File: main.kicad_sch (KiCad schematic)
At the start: 0 parts

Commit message: added motor IC
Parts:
- added U1: DRV8833PWPR, DRV8833PWPR:IC_DRV8833PWPR, symbol DRV8833PWPR[1]:DRV8833PWPR

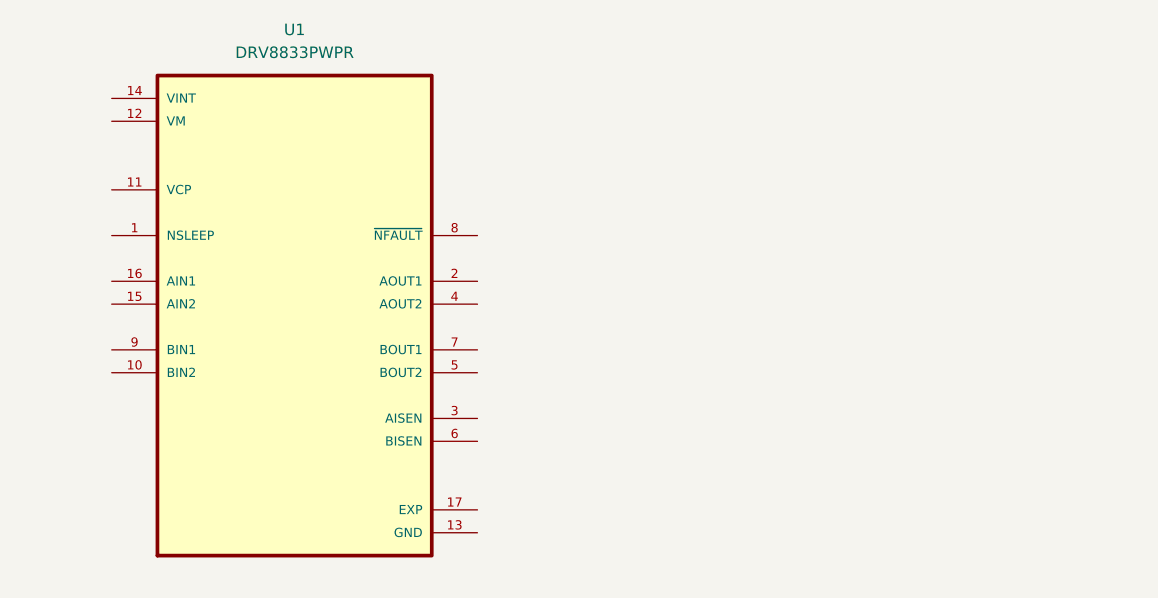
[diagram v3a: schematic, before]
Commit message: DNP for 2x16 and global labels
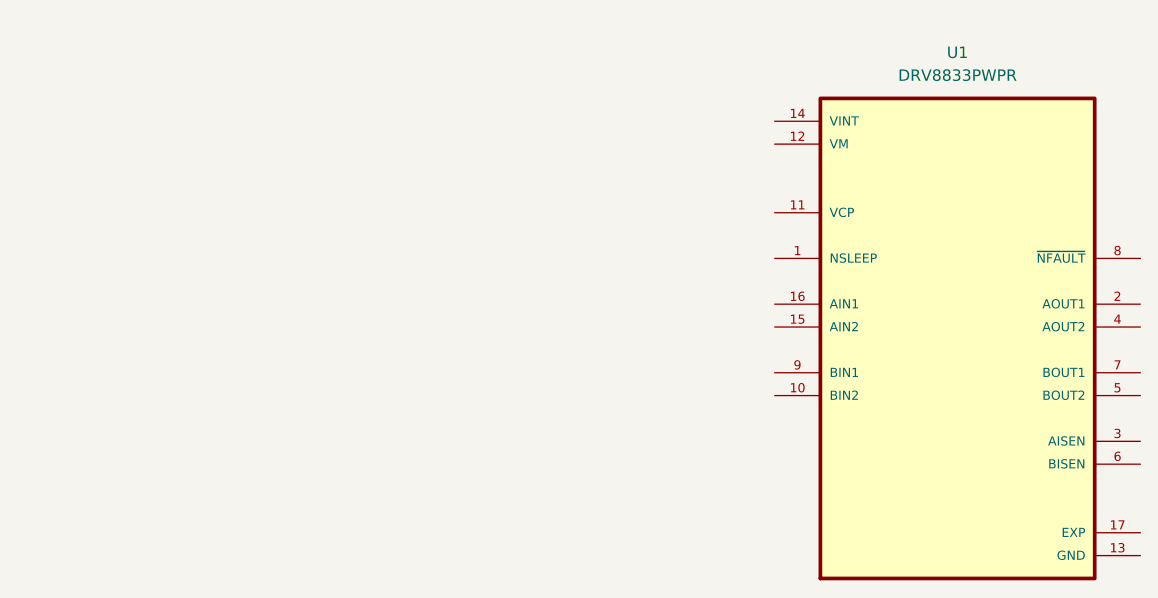
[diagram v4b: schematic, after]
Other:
- moved on the sheet: U1
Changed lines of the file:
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@@
 	(symbol
 		(lib_id "DRV8833PWPR[1]:DRV8833PWPR")
-		(at 87.63 97.79 0)
+		(at 161.29 100.33 0)
 		(unit 1)
 		(exclude_from_sim no)
@@
 		(fields_autoplaced yes)
 		(property "Reference" "U1"
-			(at 87.63 64.77 0)
+			(at 161.29 67.31 0)
 			(effects
 				(font
@@
 		)
 		(property "Value" "DRV8833PWPR"
-			(at 87.63 67.31 0)
+			(at 161.29 69.85 0)
 			(effects
 				(font
@@
 		)
 		(property "Footprint" "DRV8833PWPR:IC_DRV8833PWPR"
-			(at 87.63 97.79 0)
+			(at 161.29 100.33 0)
 			(effects
 				(font
@@
 		)
 		(property "Datasheet" ""
-			(at 87.63 97.79 0)
+			(at 161.29 100.33 0)
 			(effects
 				(font
@@
 		)
 		(property "Description" ""
-			(at 87.63 97.79 0)
+			(at 161.29 100.33 0)
 			(effects
 				(font
@@
 		)
 		(property "MF" "Texas Instruments"
-			(at 87.63 97.79 0)
+			(at 161.29 100.33 0)
 			(effects
 				(font
@@
 		)
 		(property "MOUSER-PURCHASE-URL" "https://snapeda.com/shop?store=Mouser&id=377881"
-			(at 87.63 97.79 0)
+			(at 161.29 100.33 0)
 			(effects
 				(font
@@
 		)
 		(property "DESCRIPTION" "10.8-V, 2-A dual H-bridge motor driver with current regulation 16-HTSSOP -40 to 85"
-			(at 87.63 97.79 0)
+			(at 161.29 100.33 0)
 			(effects
 				(font
@@
 		)
 		(property "PACKAGE" "HTSSOP-16 Texas Instruments"
-			(at 87.63 97.79 0)
+			(at 161.29 100.33 0)
 			(effects
 				(font
@@
 		)
 		(property "Price" "None"
-			(at 87.63 97.79 0)
+			(at 161.29 100.33 0)
 			(effects
 				(font
@@
 		)
 		(property "PRICE" "None"
-			(at 87.63 97.79 0)
+			(at 161.29 100.33 0)
 			(effects
 				(font
@@
 		)
 		(property "Package" "HTSSOP-16 Texas Instruments"
-			(at 87.63 97.79 0)
+			(at 161.29 100.33 0)
 			(effects
 				(font
@@
 		)
 		(property "Check_prices" "https://www.snapeda.com/parts/DRV8833PWPR/Texas+Instruments/view-part/?ref=eda"
-			(at 87.63 97.79 0)
+			(at 161.29 100.33 0)
 			(effects
 				(font
@@
 		)
 		(property "STANDARD" "Manufacturer Recommendations"
-			(at 87.63 97.79 0)
+			(at 161.29 100.33 0)
 			(effects
 				(font
@@
 		)
 		(property "PARTREV" "E"
-			(at 87.63 97.79 0)
+			(at 161.29 100.33 0)
 			(effects
 				(font
@@
 		)
 		(property "SnapEDA_Link" "https://www.snapeda.com/parts/DRV8833PWPR/Texas+Instruments/view-part/?ref=snap"
-			(at 87.63 97.79 0)
+			(at 161.29 100.33 0)
 			(effects
 				(font
@@
 		)
 		(property "MP" "DRV8833PWPR"
-			(at 87.63 97.79 0)
+			(at 161.29 100.33 0)
 			(effects
 				(font
@@
 		)
 		(property "TEXAS_INSTRUMENTS-PURCHASE-URL" "https://snapeda.com/shop?store=Texas+Instruments&id=377881"
-			(at 87.63 97.79 0)
+			(at 161.29 100.33 0)
 			(effects
 				(font
@@
 		)
 		(property "MAXIMUM_PACKAGE_HEIGHT" "1.2mm"
-			(at 87.63 97.79 0)
+			(at 161.29 100.33 0)
 			(effects
 				(font
@@
 		)
 		(property "Description_1" "10.8-V, 2-A dual H-bridge motor driver with current regulation"
-			(at 87.63 97.79 0)
+			(at 161.29 100.33 0)
 			(effects
 				(font
@@
 		)
 		(property "Availability" "In Stock"
-			(at 87.63 97.79 0)
+			(at 161.29 100.33 0)
 			(effects
 				(font
@@
 		)
 		(property "AVAILABILITY" "Warning"
-			(at 87.63 97.79 0)
+			(at 161.29 100.33 0)
 			(effects
 				(font
@@
 		)
 		(property "DIGIKEY-PURCHASE-URL" "https://snapeda.com/shop?store=DigiKey&id=377881"
-			(at 87.63 97.79 0)
+			(at 161.29 100.33 0)
 			(effects
 				(font
@@
 		)
 		(property "MANUFACTURER" "Texas Instruments"
-			(at 87.63 97.79 0)
-			(effects
-				(font
+			(at 161.29 100.33 0)
+			(effects
+				(font

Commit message: Removed old backups and updated KiCad files
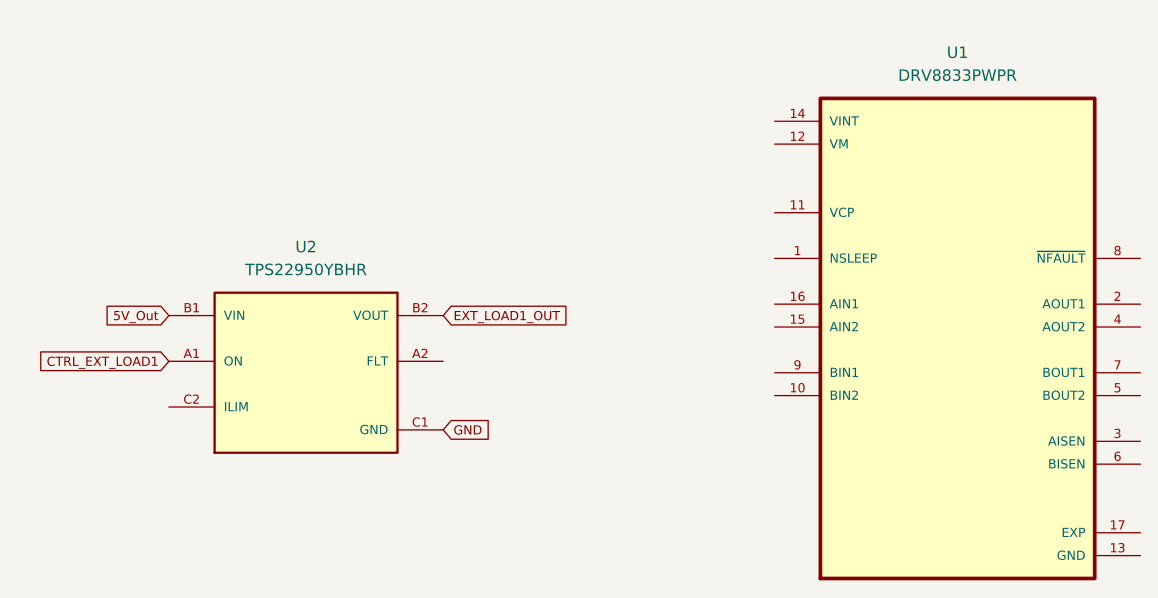
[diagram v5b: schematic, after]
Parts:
- added U2: TPS22950YBHR, TPS22950YBHR:IC_TPS22950YBHR, symbol TPS22950YBHR:TPS22950YBHR
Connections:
- new net 5V_Out: U2.B1 (VIN)
- new net CTRL_EXT_LOAD1: U2.A1 (ON)
- new net EXT_LOAD1_OUT: U2.B2 (VOUT)
- new net GND: U2.C1 (GND)
